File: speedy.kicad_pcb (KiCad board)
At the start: 2 copper layers, 49.4 x 49.4 mm, 124 parts, among them Q2 2N7002, Q3 2N7002, SW1 PushButton, U1 STM32F415RGT6, U10 LT1965, U11 INA213-SC70, U12 MCP73831, U13 DRV8839, U14 DRV8839, U2 NUF2042VX6, U4 MPU-9250, U5 MS5611-01BA, U6 VL6180X, U7 NRF24L01+, U8 LTC2955DDB-1, U9 LT1965, X1 16Mhz 10ppm, X2 16MHz 10ppm

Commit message: Replot schematic pdf for review
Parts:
- U4: footprint Housings_DFN_QFN:QFN-24-1EP_3x3mm_Pitch0.4mm -> _sensors:_MPU-9XX0
- moved C17 1.43 mm to (148.9, 95.3)
- moved C15 1.43 mm to (147.2, 95.3)
- moved C28 1.43 mm to (148.9, 94.0)
- moved C29 1.43 mm to (147.2, 93.0)
- moved C30 1.43 mm to (147.2, 94.0)
- moved L1 1.43 mm to (150.6, 93.0)
- moved L3 1.43 mm to (150.6, 94.0)
- moved L2 1.43 mm to (148.9, 93.0)
- moved C27 1.42 mm to (150.6, 95.3)
- moved R8 1.07 mm to (139.7, 104.3)
- moved R6 1.06 mm to (139.7, 102.6)
- moved C2 0.80 mm to (141.4, 107.6)
- moved U5 0.77 mm to (142.4, 104.3)
- moved R15 0.74 mm to (145.5, 101.5)
- moved C16 0.73 mm to (152.5, 98.6)
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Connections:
- U4 pad 11: Net-(U4-Pad11) -> GND
- U4 pad 19: VCC -> VCCA

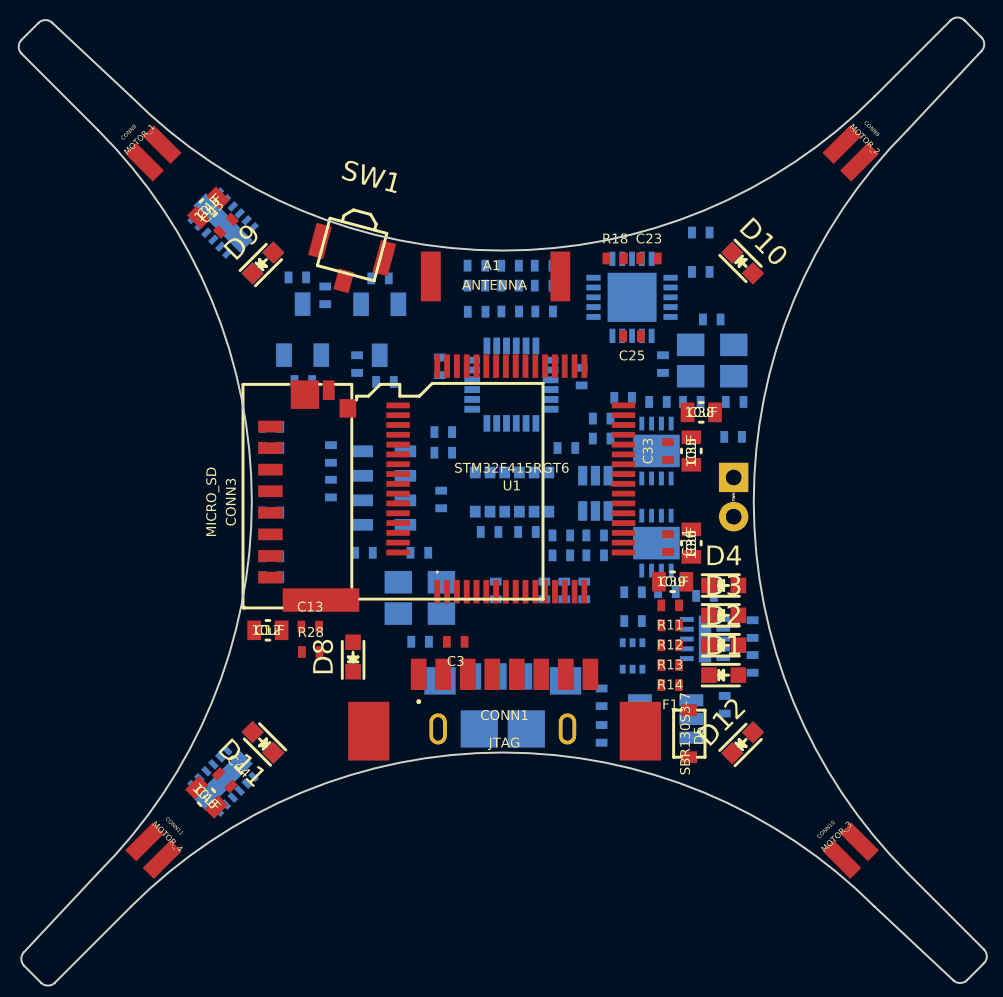
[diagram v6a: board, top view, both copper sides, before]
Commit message: (Re)Place components on PCB
Netlist was broken after review corrections
Rebuilt and placed components from scratch
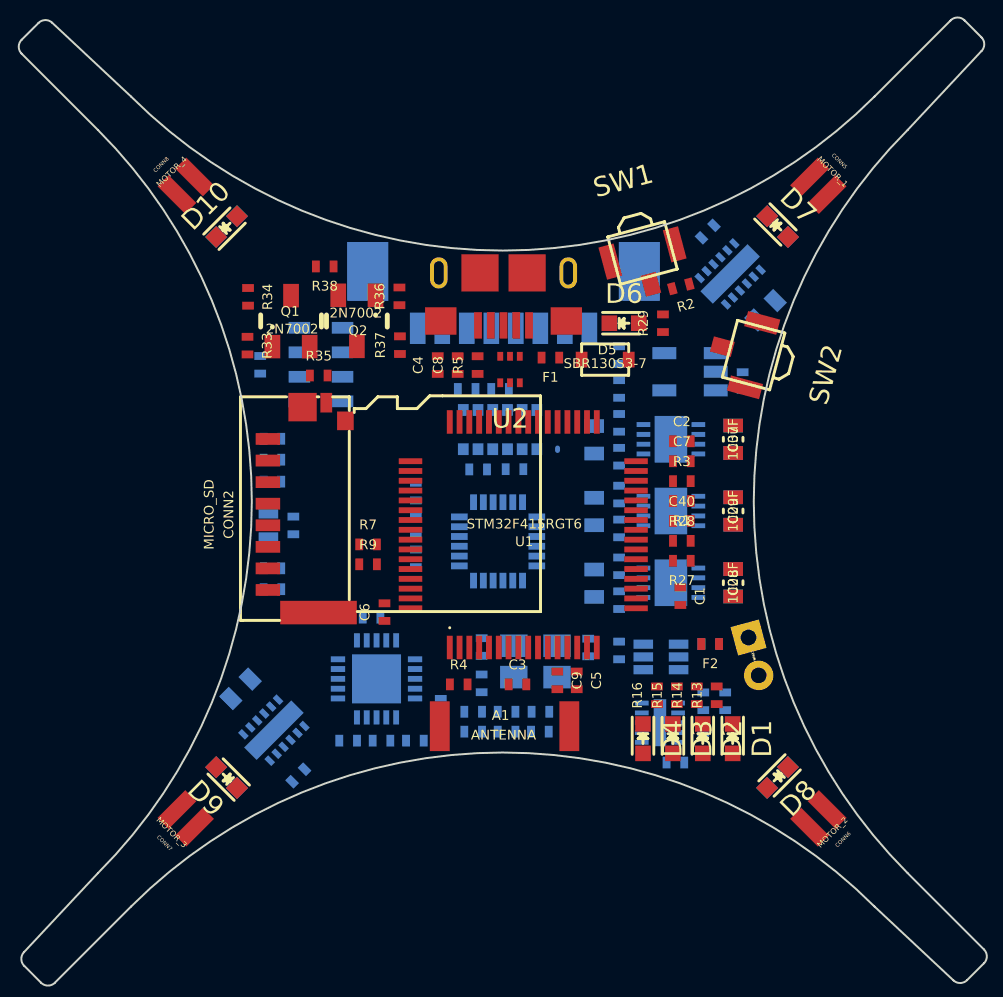
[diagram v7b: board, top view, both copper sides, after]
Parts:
- removed CONN10: MOTOR_3, _connectors:_Solder_Pad1.27_2
- removed CONN11: MOTOR_4, _connectors:_Solder_Pad1.27_2
- removed CONN9: MOTOR_2, _connectors:_Solder_Pad1.27_2
- removed D15, D16: APT1608F3C, _std:_LED_0603
- removed Q3: 2N7002, _std:_SOT23-3
- removed X2: 16MHz 10ppm, _div:_TSX-3225-SMD-XTAL
- added C14: 0.1uF, _std:_0402, B.Cu at (144.1, 104.5)
- added CONN2: MICRO_SD, _div:_Molex-microSD-WM6701, F.Cu at (136.5, 105.7)
- added CONN5: MOTOR_1, _connectors:_Solder_Pad1.27_2, F.Cu at (164.6, 88.9)
- added CONN6: MOTOR_2, _connectors:_Solder_Pad1.27_2, F.Cu at (164.6, 121.2)
- added D6: CHARGE_LED, _std:_LED_0603, F.Cu at (154.7, 95.9)
- added D7: APT1608F3C, _std:_LED_0603, F.Cu at (162.5, 91.0)
- added Q1: 2N7002, _std:_SOT23-3, F.Cu at (136.8, 97.1)
- added R10: 10k, _std:_0402, B.Cu at (136.8, 101.8)
- added R2: 47k, _std:_0402, F.Cu at (157.6, 94.0)
- added R36: 10k, _std:_0402, F.Cu at (143.2, 94.5)
- added R37: 100, _std:_0402, F.Cu at (143.3, 97.0)
- added R38: 40, _std:_0402, F.Cu at (139.4, 93.0)
- added SW2: PushButton, _div:SMD_Pushbutton_B3U-3100P, F.Cu at (161.3, 97.5)
- added U3: MPU-9250, _sensors:_MPU-9XX0, B.Cu at (148.3, 107.0)
- C1, C2, C4, C5, C6, C7, C8, C9, F2, Q2, R33, R34, R35, U2: moved to F.Cu
- C12, C13, C35, C36, C38, C43, C44, C45, C46, CONN1, D11, D12: moved to B.Cu
- C15: value 0.1uF -> 10nF
- C16: value 10nF -> 0.1uF
- C19, C41: value 0.1uF -> 4.7uF
- C20: value 4.7uF -> 0.1uF
- C21: value 0.1uF -> 33nF
- C22: value 22pF -> 10nF
- C23: value 33nF -> 1nF; moved to B.Cu
- C24: value 10nF -> 2.2nF
- C25: value 1nF -> 4.7pF; moved to B.Cu
- C26: value 22pF -> 1.5pF
- C27: value 2.2nF -> 1pF
- C28: value 4.7pF -> 100uF; footprint _std:_0402 -> _std:_0603; moved to F.Cu
- C29: value 1.5pF -> 100uF; footprint _std:_0402 -> _std:_0603; moved to F.Cu
- C30: value 1pF -> 0.1uF
- C31, C32: value 0.1uF -> 10uF; footprint _std:_0402 -> _std:_0603
- C33, C34: value 100uF -> 0.1uF; moved to B.Cu
- C37: value 0.1uF -> 100uF; footprint _std:_0402 -> _std:_0603; moved to F.Cu
- C39: value 10uF -> 4.7uF; footprint _std:_0603 -> _std:_0402; moved to B.Cu
- C40: value 4.7uF -> 0.1uF; moved to F.Cu
- C42: value 4.7uF -> 10uF; footprint _std:_0402 -> _std:_0603
- CONN3: value MICRO_SD -> MICRO_USB; footprint _div:_Molex-microSD-WM6701 -> _connectors:_Micro-USB-AB-receptacle-SMT-th
- CONN4: value MICRO_USB -> PWR; footprint _connectors:_Micro-USB-AB-receptacle-SMT-th -> _connectors:_Pin2mm_2; moved to F.Cu
- CONN7: value PWR -> MOTOR_3; footprint _connectors:_Pin2mm_2 -> _connectors:_Solder_Pad1.27_2
- CONN8: value MOTOR_1 -> MOTOR_4
- D8: value CHARGE_LED -> APT1608F3C
- R1: value 100k -> 47k; moved to F.Cu
- R11, R12: value 1k -> 10k; moved to B.Cu
- R15, R16: value 47k -> 1k; moved to F.Cu
- R17: value 1M -> 47k
- R18: value 22k -> 47k; moved to B.Cu
- R19: value 10m -> 22k
- R20: value 10k -> 10m
- R26: value 2.8k -> 10k
- R27: value 2k -> 2.8k; moved to F.Cu
- R28: value 330 -> 2k
- R29: value 2k -> 330; moved to F.Cu
- R3, R5: value 10k -> 47k; moved to F.Cu
- R30: value 10k -> 3.3k
- R31: value 100 -> 2.05k
- R32: value 40 -> 2k
- R4: value 10k -> 100k; moved to F.Cu
- R6, R8: value 4.7k -> 10k
- R7, R9: value 10k -> 4.7k; moved to F.Cu
- SW1: value PushButton -> DFU
- U10: value LT1965 -> INA213-SC70; footprint Housings_DFN_QFN:DFN-8-1EP_3x3mm_Pitch0.5mm -> _std:SC70
- U11: value INA213-SC70 -> LT1965; footprint _std:SC70 -> Housings_DFN_QFN:DFN-8-1EP_3x3mm_Pitch0.5mm
- U4: value MPU-9250 -> MS5611-01BA; footprint _sensors:_MPU-9XX0 -> _sensors:_MS5611-01BA
- U5: value MS5611-01BA -> VL6180X; footprint _sensors:_MS5611-01BA -> _sensors:VL6180X
- U6: value VL6180X -> NRF24L01+; footprint _sensors:VL6180X -> Housings_DFN_QFN:QFN-20-1EP_4x4mm_Pitch0.5mm
- U7: value NRF24L01+ -> LT1965; footprint Housings_DFN_QFN:QFN-20-1EP_4x4mm_Pitch0.5mm -> Housings_DFN_QFN:DFN-8-1EP_3x3mm_Pitch0.5mm
- U8: value LTC2955DDB-1 -> LT1965; footprint Housings_DFN_QFN:DFN-10-1EP_2x3mm_Pitch0.5mm -> Housings_DFN_QFN:DFN-8-1EP_3x3mm_Pitch0.5mm
- U9: value LT1965 -> LTC2955DDB-1; footprint Housings_DFN_QFN:DFN-8-1EP_3x3mm_Pitch0.5mm -> Housings_DFN_QFN:DFN-10-1EP_2x3mm_Pitch0.5mm
- moved D11 37.2 mm to (162.5, 91.0), turned to 315 degrees
- moved CONN7 32.4 mm to (132.3, 121.2), turned to 135 degrees
- moved C21 29.9 mm to (140.6, 117.2)
- moved C45 28.9 mm to (161.9, 95.2), turned to 225 degrees
- moved C22 27.3 mm to (142.3, 117.2)
- moved D10 26.4 mm to (134.4, 91.0), turned to 45 degrees
- moved D14 26.4 mm to (134.4, 91.0), turned to 45 degrees
- moved D13 26.3 mm to (134.4, 119.1), turned to 135 degrees
- moved D9 26.3 mm to (134.4, 119.1), turned to 135 degrees
- moved U13 26.0 mm to (160.1, 93.4), turned to 225 degrees
- moved C24 25.6 mm to (147.4, 114.3), turned to 90 degrees
- moved C43 24.6 mm to (159.0, 91.2), turned to 225 degrees
- moved C30 24.1 mm to (158.7, 115.2), turned to 90 degrees
- moved L2 23.8 mm to (147.0, 116.7), turned to 0 degrees
- moved CONN1 23.4 mm to (148.5, 93.3)
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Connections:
- net /Power/MOTOR_1_EN renamed /MOTOR_1_EN
- net /Power/MOTOR_2_EN renamed /MOTOR_2_EN
- net /Power/MOTOR_3_EN renamed /MOTOR_3_EN
- net /Power/MOTOR_3_IN renamed /MOTOR_3_IN
- net /Power/MOTOR_4_EN renamed /MOTOR_4_EN
- net /Power/MOTOR_4_IN renamed /MOTOR_4_IN
- C16 pad 1: VCCA -> Net-(C16-Pad1)
- C17 pad 1: Net-(C17-Pad1) -> VCCA
- C20 pad 1: VCCA -> VCC
- C21 pad 1: VCC -> GND
- C21 pad 2: GND -> Net-(C21-Pad2)
- C22 pad 1: Net-(C22-Pad1) -> VCC
- C23 pad 1: GND -> VCC
- C23 pad 2: Net-(C23-Pad2) -> GND
- C24 pad 1: VCC -> Net-(C24-Pad1)
- C25 pad 1: VCC -> Net-(C24-Pad1)
- C26 pad 2: GND -> Net-(A1-Pad1)
- C27 pad 1: Net-(C27-Pad1) -> Net-(A1-Pad1)
- C28 pad 1: Net-(C27-Pad1) -> +BATT
- C29 pad 1: Net-(C29-Pad1) -> +BATT
- C29 pad 2: Net-(A1-Pad1) -> GND
- C30 pad 1: Net-(A1-Pad1) -> +BATT
- C32 pad 1: Net-(C32-Pad1) -> +BATT
- C33 pad 1: +BATT -> Net-(C33-Pad1)
- C34 pad 1: +BATT -> VCC
- C35 pad 1: +BATT -> VCC
- C36 pad 1: +BATT -> VCCA
- C37 pad 1: VCC -> +BATT
- C38 pad 1: VCC -> +BATT
- C39 pad 1: VCCA -> /V_USB
- C40 pad 1: /Power/V_USB -> /VOLTAGE_BAT_SENSE
- C41 pad 1: /Power/VOLTAGE_SENSE -> +BATT
- C42 pad 1: +BATT -> SD_VCC
- CONN3 pad 1: /SDIO_D2 -> Net-(CONN3-Pad1)
- CONN3 pad 2: /SDIO_D3 -> Net-(CONN3-Pad2)
- CONN3 pad 3: /SDIO_CMD -> Net-(CONN3-Pad3)
- CONN3 pad 4: SD_VCC -> Net-(CONN3-Pad4)
- CONN3 pad 5: /SDIO_CLK -> GND
- CONN3 pad 6: GND -> Net-(CONN3-Pad6)
- CONN4 pad 2: Net-(CONN4-Pad2) -> GND
- CONN7 pad 1: Net-(CONN7-Pad1) -> /Power/MOTOR_3_OUT
- CONN8 pad 1: /Power/MOTOR_1_OUT -> /Power/MOTOR_4_OUT
- D12 pad 2: Net-(D10-Pad2) -> Net-(D12-Pad2)
- D14 pad 2: Net-(D14-Pad2) -> Net-(D12-Pad2)
- D5 pad 2: /Power/V_USB -> /V_USB
- D8 pad 1: /Power/V_USB -> Net-(D7-Pad2)
- D8 pad 2: Net-(D8-Pad2) -> Net-(D10-Pad2)
- F1 pad 2: Net-(CONN4-Pad1) -> Net-(CONN3-Pad1)
- F2 pad 1: Net-(CONN7-Pad1) -> Net-(CONN4-Pad1)
- L2 pad 2: Net-(C29-Pad1) -> Net-(C26-Pad1)
- L3 pad 2: Net-(C27-Pad1) -> Net-(C24-Pad1)
- Q2 pad 1: Net-(D10-Pad2) -> Net-(D12-Pad2)
- R1 pad 1: VCC -> GND
- R1 pad 2: /STM32F4_NRST -> /BOOT1
- R11 pad 1: Net-(D1-Pad1) -> VCC
- R11 pad 2: VCC -> /SDIO_D3
- R12 pad 1: Net-(D2-Pad1) -> VCC
- R12 pad 2: /ERROR_LED -> /SDIO_CMD
- R13 pad 1: Net-(D3-Pad1) -> Net-(D1-Pad1)
- R13 pad 2: /STATUS_LED -> VCC
- R14 pad 1: Net-(D4-Pad1) -> Net-(D2-Pad1)
- R14 pad 2: /HEARTBEAT_LED -> /ERROR_LED
- R15 pad 1: VCCA -> Net-(D3-Pad1)
- R15 pad 2: Net-(R15-Pad2) -> /STATUS_LED
- R16 pad 1: VCCA -> Net-(D4-Pad1)
- R16 pad 2: Net-(R16-Pad2) -> /HEARTBEAT_LED
- R17 pad 1: Net-(C26-Pad1) -> VCCA
- R17 pad 2: Net-(C22-Pad1) -> Net-(R17-Pad2)
- R18 pad 1: Net-(R18-Pad1) -> VCCA
- R18 pad 2: GND -> Net-(R18-Pad2)
- R19 pad 1: +BATT -> Net-(R19-Pad1)
- R19 pad 2: Net-(F2-Pad2) -> GND
- R20 pad 1: /Power/PUSHB_INT -> +BATT
- R20 pad 2: VCC -> Net-(F2-Pad2)
- R21 pad 1: /Power/POWER_KILL -> /PUSHBUTTON_INT
- R26 pad 1: +BATT -> /POWER_KILL
- R26 pad 2: /Power/VOLTAGE_SENSE -> VCC
- R27 pad 1: /Power/VOLTAGE_SENSE -> +BATT
- R27 pad 2: GND -> /VOLTAGE_BAT_SENSE
- R28 pad 1: Net-(R28-Pad1) -> /VOLTAGE_BAT_SENSE
- R28 pad 2: Net-(D8-Pad2) -> GND
- R29 pad 2: GND -> Net-(D6-Pad2)
- R3 pad 1: VCC -> /NRF24L01+_EN
- R3 pad 2: /SDIO_D0 -> GND
- R30 pad 1: /Power/IR_EN_TOP -> SD_VCC
- R30 pad 2: GND -> Net-(R30-Pad2)
- R31 pad 1: Net-(Q2-Pad2) -> Net-(R30-Pad2)
- R31 pad 2: /Power/IR_EN_TOP -> GND
- R32 pad 1: Net-(Q2-Pad3) -> Net-(R32-Pad1)
- R33 pad 1: /Power/IR_EN_BOT -> /IR_EN_TOP
- R34 pad 2: /Power/IR_EN_BOT -> /IR_EN_TOP
- R4 pad 2: /SDIO_D1 -> /STM32F4_NRST
- R5 pad 1: VCC -> /MOTOR_2_IN
- R5 pad 2: /SDIO_D2 -> GND
- R6 pad 1: VCCA -> VCC
- R6 pad 2: /Sensors/I2C1_SCL -> /SDIO_D0
- R7 pad 1: VCC -> VCCA
- R7 pad 2: /SDIO_D3 -> /I2C1_SCL
- R8 pad 1: VCCA -> VCC
- R8 pad 2: /Sensors/I2C1_SDA -> /SDIO_D1
- R9 pad 1: VCC -> VCCA
- R9 pad 2: /SDIO_CLK -> /I2C1_SDA
- SW1 pad 1: Net-(SW1-Pad1) -> /BOOT0
- SW1 pad 2: GND -> VCC
- U1 pad 15: Net-(U1-Pad15) -> /POWER_KILL
- U1 pad 16: /Power/PUSHB_INT -> /PUSHBUTTON_INT
- U1 pad 17: /Sensors/MPU9250_INT -> /MPU9250_INT
- U1 pad 20: /Sensors/MPU9250_CS -> /MPU9250_CS
- U1 pad 21: /Sensors/SPI1_SCK -> /SPI1_SCK
- U1 pad 22: /Sensors/SPI1_MISO -> /SPI1_MISO
- U1 pad 23: /Sensors/SPI1_MOSI -> /SPI1_MOSI
- U1 pad 24: /Power/CURRENT_SENSE -> /CURRENT_BAT_SENSE
- U1 pad 25: /Power/VOLTAGE_SENSE -> /VOLTAGE_BAT_SENSE
- U1 pad 28: GND -> /BOOT1
- U1 pad 29: /Wireless/NRF24L01+_INT -> /NRF24L01+_INT
- U1 pad 30: /Wireless/NRF24L01+_EN -> /NRF24L01+_EN
- U1 pad 33: /Wireless/NRF24L01+_CS -> /NRF24L01+_CS
- U1 pad 34: /Wireless/SPI2_SCK -> /SPI2_SCK
- U1 pad 35: /Wireless/SPI2_MISO -> /SPI2_MISO
- U1 pad 36: /Wireless/SPI2_MOSI -> /SPI2_MOSI
- U1 pad 41: /Power/MOTOR_1_IN -> /MCU_OSC_OUT
- U1 pad 42: /Power/MOTOR_2_IN -> /MOTOR_1_IN
- U1 pad 43: /Power/POWER_KILL -> /MOTOR_2_IN
- U1 pad 58: /Sensors/I2C1_SCL -> /I2C1_SCL
- U1 pad 59: /Sensors/I2C1_SDA -> /I2C1_SDA
- U1 pad 60: VCC -> /BOOT0
- U1 pad 61: /Power/IR_EN_TOP -> /IR_EN_TOP
- U1 pad 62: /Power/IR_EN_BOT -> /IR_EN_BOTTOM
- U1 pad 8: /Power/SENSOR_EN -> /SENSOR_PWR_ON
- U10 pad 1: VCCA -> GND
- U10 pad 2: VCCA -> GND
- U10 pad 3: Net-(R24-Pad2) -> VCC
- U10 pad 4: GND -> +BATT
- U10 pad 5: GND -> Net-(F2-Pad2)
- U10 pad 6: /Power/SENSOR_EN -> /CURRENT_BAT_SENSE
- U11 pad 1: GND -> SD_VCC
- U11 pad 2: GND -> SD_VCC
- U11 pad 3: VCC -> Net-(R30-Pad2)
- U11 pad 4: +BATT -> GND
- U11 pad 5: Net-(F2-Pad2) -> GND
- U11 pad 6: /Power/CURRENT_SENSE -> /SD_PWR_EN
- U12 pad 1: Net-(R28-Pad1) -> Net-(R29-Pad1)
- U12 pad 4: /Power/V_USB -> /V_USB
- U12 pad 5: Net-(R29-Pad1) -> Net-(R32-Pad1)
- U13 pad 10: /Power/MOTOR_1_IN -> /MOTOR_1_IN
- U13 pad 8: /Power/MOTOR_2_IN -> /MOTOR_2_IN
- U2 pad 4: Net-(CONN4-Pad2) -> Net-(CONN3-Pad2)
- U2 pad 5: /Power/V_USB -> /V_USB
- U2 pad 6: Net-(CONN4-Pad3) -> Net-(CONN3-Pad3)
- U4 pad 1: Net-(U4-Pad1) -> VCCA
- U4 pad 2: Net-(U4-Pad2) -> VCCA
- U4 pad 3: Net-(U4-Pad3) -> GND
- U4 pad 4: Net-(U4-Pad4) -> GND
- U4 pad 5: Net-(U4-Pad5) -> GND
- U4 pad 7: Net-(U4-Pad7) -> /I2C1_SDA
- U4 pad 8: VCCA -> /I2C1_SCL
- U5 pad 1: VCCA -> Net-(R18-Pad2)
- U5 pad 2: VCCA -> Net-(U5-Pad2)
- U5 pad 3: GND -> Net-(U5-Pad3)
- U5 pad 4: GND -> Net-(R17-Pad2)
- U5 pad 5: GND -> /I2C1_SCL
- U5 pad 6: Net-(U5-Pad6) -> /I2C1_SDA
- U5 pad 7: /Sensors/I2C1_SDA -> Net-(U5-Pad7)
- U5 pad 8: /Sensors/I2C1_SCL -> VCCA
- U6 pad 1: Net-(R16-Pad2) -> /NRF24L01+_EN
- U6 pad 10: VCCA -> /MCU_OSC_OUT
- U6 pad 11: Net-(U6-Pad11) -> Net-(C24-Pad1)
- U6 pad 12: GND -> Net-(L1-Pad2)
- U6 pad 2: Net-(U6-Pad2) -> /NRF24L01+_CS
- U6 pad 3: Net-(U6-Pad3) -> /SPI2_SCK
- U6 pad 4: Net-(R15-Pad2) -> /SPI2_MOSI
- U6 pad 5: /Sensors/I2C1_SCL -> /SPI2_MISO
- U6 pad 6: /Sensors/I2C1_SDA -> /NRF24L01+_INT
- U6 pad 7: Net-(U6-Pad7) -> VCC
- U6 pad 8: VCCA -> GND
- U6 pad 9: GND -> Net-(U6-Pad9)
- U7 pad 1: /Wireless/NRF24L01+_EN -> VCC
- U7 pad 2: /Wireless/NRF24L01+_CS -> VCC
- U7 pad 3: /Wireless/SPI2_SCK -> Net-(R22-Pad2)
- U7 pad 4: /Wireless/SPI2_MOSI -> GND
- U7 pad 5: /Wireless/SPI2_MISO -> GND
- U7 pad 6: /Wireless/NRF24L01+_INT -> /Power/POWER_EN
- U7 pad 7: VCC -> +BATT
- U7 pad 8: GND -> +BATT
- U7 pad 9: Net-(C22-Pad1) -> GND
- U8 pad 1: /Power/PUSHB_INT -> VCCA
- U8 pad 2: Net-(U8-Pad2) -> VCCA
- U8 pad 3: /Power/POWER_EN -> Net-(R24-Pad2)
- U8 pad 4: +BATT -> GND
- U8 pad 5: Net-(SW1-Pad1) -> GND
- U8 pad 6: GND -> /SENSOR_PWR_ON
- U8 pad 8: Net-(C32-Pad1) -> +BATT
- U8 pad 9: /Power/POWER_KILL -> GND
- U9 pad 1: VCC -> /PUSHBUTTON_INT
- U9 pad 2: VCC -> Net-(U9-Pad2)
- U9 pad 3: Net-(R22-Pad2) -> /Power/POWER_EN
- U9 pad 4: GND -> +BATT
- U9 pad 5: GND -> Net-(SW2-Pad1)
- U9 pad 6: /Power/POWER_EN -> GND
- U9 pad 8: +BATT -> Net-(C33-Pad1)
- U9 pad 9: GND -> /POWER_KILL

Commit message: Update form to square PCB, place components and update 3D models
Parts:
- C10, C11, C14, C15, C16, C17, C20, C21, C22, C23, C24, C25, C26, C27, C39, C41, L1, L2, L3, R19, R32, U12, U3, U4, U6, X1: moved to F.Cu
- C18: value 0.1uF -> 4.7uF
- C19: value 4.7uF -> 0.1uF
- C28, C29, C37, C40, C5, F2, Q2, R27, R28, R36, R37, R38, R4, R7, R9: moved to B.Cu
- CONN1: value JTAG -> SWD/DEBUG; footprint _connectors:_Molex-PicoBlade-SMD-8 -> _connectors:_Molex-PicoBlade-SMD-7
- R17, R18: value 47k -> 10k
- SW2: value PushButton -> Push
- U5: value VL6180X -> VL53L0X; footprint _sensors:VL6180X -> _sensors:ST-VL53L0X
- moved CONN8 42.8 mm to (160.2, 121.4), turned to 270 degrees
- moved CONN7 40.0 mm to (160.2, 92.3), turned to 90 degrees
- moved D10 36.8 mm to (160.7, 116.8), turned to 90 degrees
- moved D14 36.8 mm to (160.7, 116.8), turned to 90 degrees
- moved D9 34.4 mm to (160.7, 96.8), turned to 270 degrees
- moved D13 34.4 mm to (160.7, 96.9), turned to 270 degrees
- moved SW1 34.1 mm to (138.2, 121.6), turned to 180 degrees
- moved CONN5 33.6 mm to (131.2, 92.4), turned to 90 degrees
- moved CONN6 33.4 mm to (131.2, 121.3), turned to 270 degrees
- moved C41 32.8 mm to (133.6, 117.2)
- moved D11 32.4 mm to (130.7, 96.8), turned to 270 degrees
- moved D7 32.4 mm to (130.7, 96.8), turned to 270 degrees
- moved D8 31.9 mm to (130.7, 116.8), turned to 90 degrees
- moved D12 31.9 mm to (130.7, 116.9), turned to 90 degrees
- moved C37 30.7 mm to (132.3, 114.8), turned to 270 degrees
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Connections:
- CONN1 pad 4: /STM32F4_TRST -> /STM32F4_SWDIO
- CONN1 pad 5: /STM32F4_TDI -> /STM32F4_SWCLK
- CONN1 pad 6: /STM32F4_TDO -> /UART3_TX
- CONN1 pad 7: /STM32F4_TMS -> /UART3_RX
- R17 pad 2: Net-(R17-Pad2) -> /TOF_XSHUT
- R18 pad 2: Net-(R18-Pad2) -> /TOF_GPIO1
- U1 pad 14: Net-(U1-Pad14) -> /TOF_XSHUT
- U1 pad 29: /NRF24L01+_INT -> /UART3_TX
- U1 pad 30: /NRF24L01+_EN -> /UART3_RX
- U1 pad 46: /STM32F4_TMS -> /STM32F4_SWDIO
- U1 pad 49: /STM32F4_TCK -> /STM32F4_SWCLK
- U1 pad 50: /STM32F4_TDI -> /TOF_GPIO1
- U1 pad 55: /STM32F4_TDO -> /NRF24L01+_INT
- U1 pad 56: /STM32F4_TRST -> /NRF24L01+_EN
- U5 pad 1: Net-(R18-Pad2) -> VCCA
- U5 pad 10: VCCA -> /I2C1_SCL
- U5 pad 11: Net-(U5-Pad11) -> VCCA
- U5 pad 2: Net-(U5-Pad2) -> GND
- U5 pad 3: Net-(U5-Pad3) -> GND
- U5 pad 4: Net-(R17-Pad2) -> GND
- U5 pad 5: /I2C1_SCL -> /TOF_XSHUT
- U5 pad 6: /I2C1_SDA -> GND
- U5 pad 7: Net-(U5-Pad7) -> /TOF_GPIO1
- U5 pad 8: VCCA -> Net-(U5-Pad8)
- U5 pad 9: GND -> /I2C1_SDA
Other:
- board size 49.4 x 49.4 mm -> 32 x 32 mm
